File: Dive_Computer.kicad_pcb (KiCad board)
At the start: 2 copper layers, 4 parts, among them IC1 LTC4120EUD-4.2#PBF, IC2 MS583730BA01-50, U1 ESP32-C3_SUPERMINI_TH

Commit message: Schematic update
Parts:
- added BATTERIE1: BAT, Connector_Hirose:Hirose_DF13-02P-1.25DSA_1x02_P1.25mm_Vertical, F.Cu at (142.6, 100.2)
- added C1: 10u, Capacitor_SMD:C_1210_3225Metric, F.Cu at (142.9, 104.5)
- added C10: 100n, Capacitor_SMD:C_0603_1608Metric, F.Cu at (146.1, 83.1)
- added C2: 100n, Capacitor_SMD:C_0603_1608Metric, F.Cu at (142.1, 83.1)
- added C3: 10u, Capacitor_SMD:C_1210_3225Metric, F.Cu at (142.9, 108.8)
- added C4: 26.7n, Capacitor_SMD:C_0603_1608Metric, F.Cu at (142.1, 85.6)
- added C5: 6.5n, Capacitor_SMD:C_0603_1608Metric, F.Cu at (142.1, 88.2)
- added C6: 22u, Capacitor_SMD:C_1210_3225Metric, F.Cu at (142.9, 113.0)
- added C7: 22n, Capacitor_SMD:C_0603_1608Metric, F.Cu at (142.1, 90.7)
- added C8: 2.2u, Capacitor_SMD:C_0603_1608Metric, F.Cu at (142.1, 93.2)
- added C9: 100n, Capacitor_SMD:C_0603_1608Metric, F.Cu at (142.1, 95.7)
- added D1: MSS2P2-M3/89A, Diode_SMD:D_MicroSMP_LargeCathode, F.Cu at (154.8, 83.3)
- added D2: MSS2P2-M3/89A, Diode_SMD:D_MicroSMP_LargeCathode, F.Cu at (154.8, 86.2)
- added D3: MSS2P2-M3/89A, Diode_SMD:D_MicroSMP_LargeCathode, F.Cu at (154.8, 89.0)
- added D4: MSS2P2-M3/89A, Diode_SMD:D_MicroSMP_LargeCathode, F.Cu at (154.8, 91.9)
- added J1: SCREEN, Connector_Hirose:Hirose_DF13-07P-1.25DSA_1x07_P1.25mm_Vertical, F.Cu at (123.0, 110.7)
- added JP1: SolderJumper_2_Open, Jumper:SolderJumper-2_P1.3mm_Open_RoundedPad1.0x1.5mm, F.Cu at (153.0, 114.2)
- added L1: 15u, Inductor_SMD:L_APV_ANR4018, F.Cu at (148.6, 105.2)
- added Power_Inductor1: 47.0 uH, Connector_PinHeader_2.54mm:PinHeader_1x02_P2.54mm_Vertical, F.Cu at (109.8, 109.8)
- added Q1: Si2301HDS, Package_TO_SOT_SMD:TSOT-23, F.Cu at (154.1, 104.8)
- added R1: 10k, Resistor_SMD:R_0603_1608Metric, F.Cu at (146.1, 85.6)
- added R10: 10k, Resistor_SMD:R_0603_1608Metric, F.Cu at (150.1, 93.2)
- added R2: 10k, Resistor_SMD:R_0603_1608Metric, F.Cu at (146.1, 88.2)
- added R3: 3k, Resistor_SMD:R_0603_1608Metric, F.Cu at (146.1, 90.7)
- added R4: 300k, Resistor_SMD:R_0603_1608Metric, F.Cu at (146.1, 93.2)
- added R5: 100k, Resistor_SMD:R_0603_1608Metric, F.Cu at (146.1, 95.7)
- added R6: 10k, Resistor_SMD:R_0603_1608Metric, F.Cu at (150.1, 83.1)
- added R7: 10k, Resistor_SMD:R_0603_1608Metric, F.Cu at (150.1, 85.6)
- added R8: 10k, Resistor_SMD:R_0603_1608Metric, F.Cu at (150.1, 88.2)
- added R9: 10k, Resistor_SMD:R_0603_1608Metric, F.Cu at (150.1, 90.7)
- added U2: Si7201-03-IV, Package_TO_SOT_SMD:SOT-23, F.Cu at (153.3, 110.2)
- IC1: footprint SamacSys_Parts:QFN50P300X300X80-17N-D -> Package_DFN_QFN:QFN-16-1EP_3x3mm_P0.5mm_EP1.7x1.7mm
- IC2: footprint SamacSys_Parts:MS583730BA0150 -> Sensor_Pressure:TE_MS5837-xxBA
- moved U1 67.7 mm to (113.5, 80.9)
- moved IC2 42.1 mm to (148.4, 110.6)
- moved IC1 38.7 mm to (149.3, 99.6)
- moved LIS12DUX1 24.8 mm to (162.3, 109.7)
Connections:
- IC1 pad 1: unconnected-(IC1-INTVCC-Pad1) -> Net-(IC1-FREQ)
- IC1 pad 10: unconnected-(IC1-BATSNS-Pad10) -> VCC
- IC1 pad 12: unconnected-(IC1-NTC-Pad12) -> GND
- IC1 pad 13: unconnected-(IC1-PROG-Pad13) -> Net-(IC1-PROG)
- IC1 pad 14: unconnected-(IC1-~{CHRG}-Pad14) -> /~{CHRG}
- IC1 pad 15: unconnected-(IC1-~{FAULT}-Pad15) -> /~{FLT}
- IC1 pad 16: unconnected-(IC1-RUN-Pad16) -> Net-(D2-K)
- IC1 pad 17: unconnected-(IC1-GND_2-Pad17) -> GND
- IC1 pad 2: unconnected-(IC1-BOOST-Pad2) -> Net-(IC1-BOOST)
- IC1 pad 3: unconnected-(IC1-IN-Pad3) -> Net-(D2-K)
- IC1 pad 4: unconnected-(IC1-SW-Pad4) -> Net-(IC1-SW)
- IC1 pad 5: unconnected-(IC1-GND_1-Pad5) -> GND
- IC1 pad 6: unconnected-(IC1-DHC-Pad6) -> Net-(D2-A)
- IC1 pad 7: unconnected-(IC1-FREQ-Pad7) -> Net-(IC1-FREQ)
- IC1 pad 8: unconnected-(IC1-CHGSNS-Pad8) -> Net-(IC1-CHGSNS)
- IC1 pad 9: unconnected-(IC1-BAT-Pad9) -> VCC
- IC2 pad 1: unconnected-(IC2-GND-Pad1) -> GND
- IC2 pad 2: unconnected-(IC2-VDD-Pad2) -> +3.3V
- IC2 pad 3: unconnected-(IC2-SCL-Pad3) -> /SCL
- IC2 pad 4: unconnected-(IC2-SDA-Pad4) -> /SDA
- LIS12DUX1 pad 1: unconnected-(LIS12DUX1-SCL-Pad1) -> /SCL
- LIS12DUX1 pad 10: unconnected-(LIS12DUX1-Vdd_IO-Pad10) -> +3.3V
- LIS12DUX1 pad 11: unconnected-(LIS12DUX1-INT2-Pad11) -> /INT2
- LIS12DUX1 pad 12: unconnected-(LIS12DUX1-INT1-Pad12) -> /INT1
- LIS12DUX1 pad 2: unconnected-(LIS12DUX1-CS-Pad2) -> +3.3V
- LIS12DUX1 pad 3: unconnected-(LIS12DUX1-SDO-Pad3) -> +3.3V
- LIS12DUX1 pad 4: unconnected-(LIS12DUX1-SDA-Pad4) -> /SDA
- LIS12DUX1 pad 6: unconnected-(LIS12DUX1-GND-Pad6) -> GND
- LIS12DUX1 pad 7: unconnected-(LIS12DUX1-RES-Pad7) -> GND
- LIS12DUX1 pad 8: unconnected-(LIS12DUX1-GND-Pad8) -> GND
- LIS12DUX1 pad 9: unconnected-(LIS12DUX1-Vdd-Pad9) -> +3.3V
- U1 pad 0: unconnected-(U1-GPIO0-Pad0) -> /INT1
- U1 pad 1: unconnected-(U1-GPIO1-Pad1) -> /INT2
- U1 pad 10: unconnected-(U1-GPIO10-Pad10) -> /Data/Command
- U1 pad 20: unconnected-(U1-GPIO20-Pad20) -> /~{CHRG}
- U1 pad 21: unconnected-(U1-GPIO21-Pad21) -> Net-(JP1-A)
- U1 pad 3: unconnected-(U1-GPIO3-Pad3) -> Net-(U1-GPIO3)
- U1 pad 3.3: unconnected-(U1-3V3-Pad3.3) -> +3.3V
- U1 pad 4: unconnected-(U1-GPIO4-Pad4) -> /SPI_CLK
- U1 pad 5: unconnected-(U1-GPIO5-Pad5) -> /MISO
- U1 pad 5V: unconnected-(U1-Pad5V) -> Net-(D4-K)
- U1 pad 6: unconnected-(U1-GPIO6-Pad6) -> /MOSI
- U1 pad 7: unconnected-(U1-GPIO7-Pad7) -> /CS
- U1 pad 8: unconnected-(U1-GPIO8-Pad8) -> /SDA
- U1 pad 9: unconnected-(U1-GPIO9-Pad9) -> /SCL
- U1 pad G: unconnected-(U1-GND-PadG) -> GND

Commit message: Routage terminé
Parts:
- added ?: , , F.Cu at (206.7, 55.5)
- added ?: , , F.Cu at (244.8, 55.5)
- added ?: , , F.Cu at (206.7, 86.0)
- added ?: , , F.Cu at (244.8, 86.0)
- added G***: LOGO, LOGO, B.Cu at (223.0, 74.3)
- C1, C6: footprint Capacitor_SMD:C_1210_3225Metric -> Capacitor_SMD:C_0603_1608Metric
- IC2: moved to B.Cu
- moved U1 120.7 mm to (233.8, 70.7), turned to -90 degrees
- moved Power_Inductor1 113.5 mm to (220.7, 85.6), turned to -90 degrees
- moved J1 113.1 mm to (221.9, 55.9)
- moved IC2 103.2 mm to (237.5, 58.5), turned to -90 degrees
- moved C3 98.1 mm to (238.1, 85.0)
- moved C10 95.5 mm to (237.5, 55.3)
- moved C8 93.1 mm to (234.4, 80.8)
- moved R4 93.1 mm to (238.5, 81.7), turned to 90 degrees
- moved C6 93.0 mm to (232.1, 86.7)
- moved R2 93.0 mm to (234.4, 59.0), turned to 90 degrees
- moved R6 92.1 mm to (242.2, 81.6), turned to -90 degrees
- moved R5 91.9 mm to (236.9, 81.7), turned to -90 degrees
- moved JP1 91.0 mm to (225.9, 59.8), turned to 90 degrees
- moved R7 90.6 mm to (240.6, 81.6), turned to 90 degrees
- moved R1 90.6 mm to (232.7, 58.9), turned to 90 degrees
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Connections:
- C3 pad 1: Net-(D2-K) -> Net-(IC1-RUN)
- IC1 pad 16: Net-(D2-K) -> Net-(IC1-RUN)
- J1 pad 2: /BAT+ -> VCC
- Power_Inductor1 pad 1: Net-(C4-Pad1) -> GND
- Power_Inductor1 pad 2: GND -> Net-(C4-Pad1)
- R4 pad 1: Net-(D2-K) -> Net-(IC1-RUN)
- R5 pad 2: Net-(D2-K) -> Net-(IC1-RUN)
- R6 pad 2: /BAT+ -> VCC
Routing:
- net /SCL: track 0.00 -> 50.5 mm
- net VCC: track 0.00 -> 42.5 mm, vias 0 -> 5
- net /SDA: track 0.00 -> 34.4 mm
- net /~{FLT}: track 0.00 -> 32.0 mm, vias 0 -> 2
- net /~{CHRG}: track 0.00 -> 28.6 mm, vias 0 -> 1
- net /SPI_CLK: track 0.00 -> 26.7 mm
- net /INT2: track 0.00 -> 26.5 mm
- net /INT1: track 0.00 -> 21.2 mm
- net /MISO: track 0.00 -> 20.4 mm
- net Net-(D2-K): track 0.00 -> 19.9 mm, vias 0 -> 3
- net Net-(Q1-G): track 0.00 -> 18.7 mm
- net Net-(D2-A): track 0.00 -> 17.0 mm
- net /MOSI: track 0.00 -> 15.8 mm
- net /CS: track 0.00 -> 15.7 mm
- net Net-(U1-GPIO3): track 0.00 -> 13.0 mm
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- added copper zone on F.Cu, net +3.3V
- added copper zone on In1.Cu, net +3.3V
- added copper zone on F.Cu, net /BAT+
- added copper zone on B.Cu, net GND
- added copper zone on F.Cu, net GND
- added copper zone on In1.Cu, net GND
- added copper zone on In2.Cu, net GND
- added copper zone on F.Cu, net Net-(C4-Pad1)
- added copper zone on F.Cu, net Net-(D1-K)
- added copper zone on F.Cu, net Net-(D2-K)
- added copper zone on In2.Cu, net Net-(D2-K)
- added copper zone on F.Cu, net Net-(D4-K)
- added copper zone on F.Cu, net Net-(IC1-CHGSNS)
- added copper zone on F.Cu, net Net-(IC1-RUN)
- added copper zone on F.Cu, net Net-(IC1-SW)
- added copper zone on F.Cu, net VCC
- added copper zone on In1.Cu, net VCC
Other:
- board outline added: 42.1 x 34.5 mm
- copper layers 2 -> 4
- board text added: "ESP32C3 SUPERMINI"
- board text added: "Freediving Computer V1 Design by Bilal Yousfi"

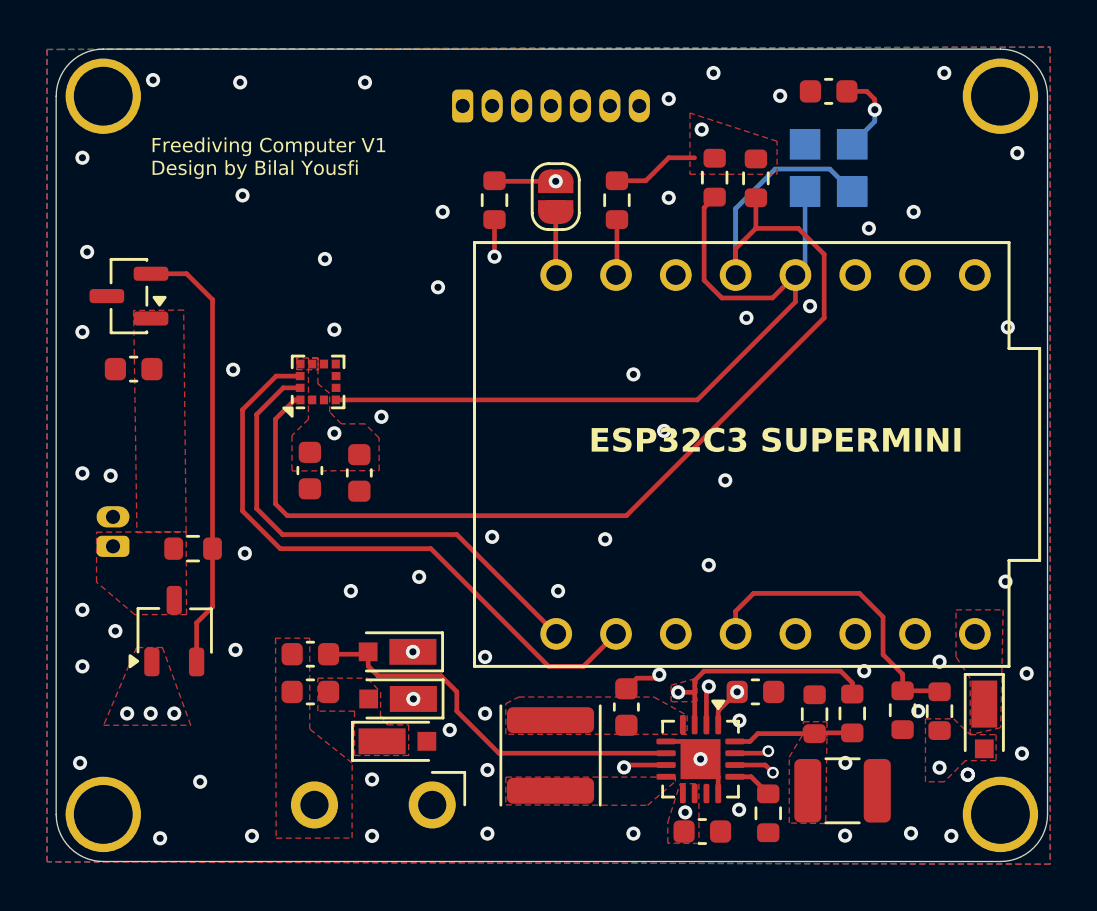
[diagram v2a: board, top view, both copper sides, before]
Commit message: Added 3D models
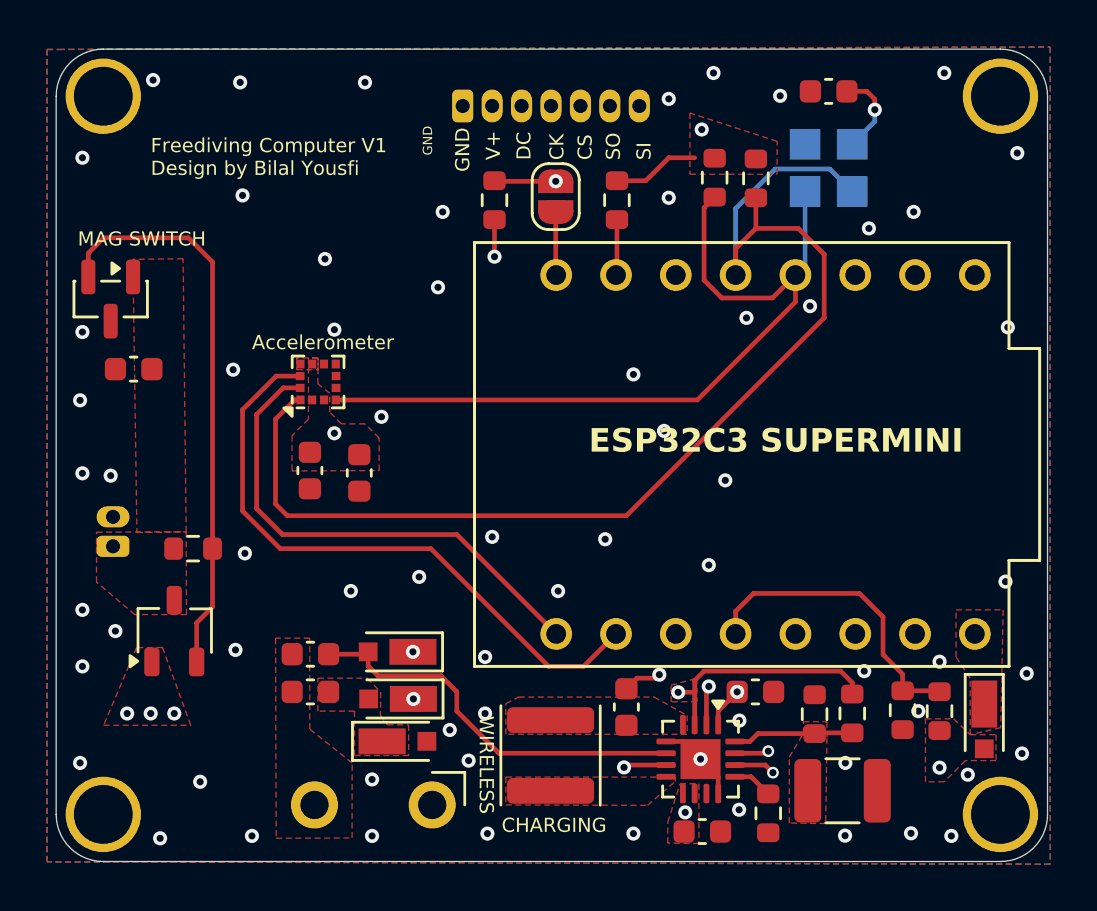
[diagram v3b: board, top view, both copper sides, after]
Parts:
- moved U2 0.79 mm to (207.0, 64.1), turned to -90 degrees
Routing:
- net Net-(Q1-G): track 18.7 -> 24.2 mm
- net GND: vias 67 -> 66
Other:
- board text added: "Accelerometer"
- board text added: "CHARGING"
- board text added: "CK"
- board text added: "CS"
- board text added: "DC"
- board text added: "GND"
- board text added: "MAG SWITCH"
- board text added: "SI"
- board text added: "SO"
- board text added: "V+"
- board text added: "WIRELESS"

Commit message: UI
The UI is mostly done
The core architecture is up and running
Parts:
- moved U2 0.10 mm to (207.0, 64.0)
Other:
- board text removed: "Accelerometer"
- board text removed: "CHARGING"
- board text removed: "CK"
- board text removed: "CS"
- board text removed: "DC"
- board text removed: "GND"
- board text removed: "MAG SWITCH"
- board text removed: "SI"
- board text removed: "SO"
- board text removed: "V+"
- board text removed: "WIRELESS"
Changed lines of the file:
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@@
 			(outputformat 1)
 			(mirror no)
-			(drillshape 0)
+			(drillshape 1)
 			(scaleselection 1)
 			(outputdirectory "")
@@
 			)
 		)
-		(model "${KIPRJMOD}/3d files/MSMP20A-M3_89A.STEP"
+		(model "${KICAD10_3DMODEL_DIR}/Custom/MSMP20A-M3_89A.STEP"
 			(offset
 				(xyz 0 0 0)
@@
 	(footprint "Package_TO_SOT_SMD:SOT-23"
 		(layer "F.Cu")
-		(at 207 64.1 -90)
+		(at 207 64 -90)
 		(descr "SOT, 3 Pin (JEDEC TO-236 Var AB https://www.jedec.org/document_search?search_api_views_fulltext=TO-236)")
 		(tags "SOT TO_SOT_SMD")
@@
 		)
 		(embedded_fonts no)
-		(model "${KIPRJMOD}/3d files/ESP32-C3 SuperMini_TH--3DModel-STEP-56544.STEP"
+		(model "${KICAD10_3DMODEL_DIR}/Custom/ESP32-C3 SuperMini_TH--3DModel-STEP-56544.STEP"
 			(offset
 				(xyz 0 0 0)
@@
 			)
 			(rotate
-				(xyz 0 0 0)
+				(xyz -90 -0 -0)
 			)
 		)
-		(model "${KIPRJMOD}/3d files/MSMP20A-M3_89A.STEP"
+		(model "${KICAD10_3DMODEL_DIR}/Custom/MSMP20A-M3_89A.STEP"
 			(offset
 				(xyz 0 0 0)
@@
 			)
 		)
-		(model "${KIPRJMOD}/3d files/MSMP20A-M3_89A.STEP"
+		(model "${KICAD10_3DMODEL_DIR}/Custom/MSMP20A-M3_89A.STEP"
 			(offset
 				(xyz 0 0 0)
@@
 			)
 		)
-		(model "${KIPRJMOD}/3d files/MSMP20A-M3_89A.STEP"
+		(model "${KICAD10_3DMODEL_DIR}/Custom/MSMP20A-M3_89A.STEP"
 			(offset
 				(xyz 0 0 0)
@@
 			)
 		)
-		(model "${KIPRJMOD}/3d files/MS583730BA01-50--3DModel-STEP-510211.STEP"
+		(model "${KICAD10_3DMODEL_DIR}/Custom/MS583730BA01-50--3DModel-STEP-510211.STEP"
 			(offset
 				(xyz 0 0 0)
@@
 		(layer "B.Fab")
 	)
-	(gr_text "GND"
-		(at 220.7 58 90)
-		(layer "F.SilkS")
-		(effects
-			(font
-				(size 0.4 0.4)
-			)
-			(justify left bottom)
-		)
-	)
-	(gr_text "MAG SWITCH"
-		(at 205.6 61.9 0)
-		(layer "F.SilkS")
-		(effects
-			(font
-				(size 0.6 0.6)
-			)
-			(justify left bottom)
-		)
-	)
 	(gr_text "Freediving Computer V1\nDesign by Bilal Yousfi"
 		(at 208.7 58.9 0)
@@
 		)
 	)
-	(gr_text "Accelerometer"
-		(at 213 66.3 0)
-		(layer "F.SilkS")
-		(effects
-			(font
-				(size 0.6 0.6)
-			)
-			(justify left bottom)
-		)
-	)
-	(gr_text "CHARGING"
-		(at 223.6 86.8 0)
-		(layer "F.SilkS")
-		(effects
-			(font
-				(size 0.6 0.6)
-			)
-			(justify left bottom)
-		)
-	)
-	(gr_text "GND"
-		(at 222.3 58.7 90)
-		(layer "F.SilkS")
-		(effects
-			(font
-				(size 0.6 0.6)
-			)
-			(justify left bottom)
-		)
-	)
-	(gr_text "V+"
-		(at 223.6 58.2 90)
-		(layer "F.SilkS")
-		(effects
-			(font
-				(size 0.6 0.6)
-			)
-			(justify left bottom)
-		)
-	)
-	(gr_text "DC"
-		(at 224.9 58.2 90)
-		(layer "F.SilkS")
-		(effects
-			(font
-				(size 0.6 0.6)
-			)
-			(justify left bottom)
-		)
-	)
-	(gr_text "CK"
-		(at 226.3 58.2 90)
-		(layer "F.SilkS")
-		(effects
-			(font
-				(size 0.6 0.6)
-			)
-			(justify left bottom)
-		)
-	)
-	(gr_text "CS"
-		(at 227.5 58.2 90)
-		(layer "F.SilkS")
-		(effects
-			(font
-				(size 0.6 0.6)
-			)
-			(justify left bottom)
-		)
-	)
-	(gr_text "SO"
-		(at 228.7 58.2 90)
-		(layer "F.SilkS")
-		(effects
-			(font
-				(size 0.6 0.6)
-			)
-			(justify left bottom)
-		)
-	)
-	(gr_text "SI"
-		(at 230 58.2 90)
-		(layer "F.SilkS")
-		(effects
-			(font
-				(size 0.6 0.6)
-			)
-			(justify left bottom)
-		)
-	)
-	(gr_text "WIRELESS"
-		(at 222.6 81.8 270)
-		(layer "F.SilkS")
-		(effects
-			(font
-				(size 0.6 0.6)
-			)
-			(justify left bottom)
-		)
-	)
 	(gr_text "ESP32C3 SUPERMINI"
 		(at 227.3 70.7 0)
@@
 	)
 	(via
+		(at 205.8 65.5)
+		(size 0.6)
+		(drill 0.3)
+		(layers "F.Cu" "B.Cu")
+		(free yes)
+		(net "GND")
+	)
+	(via
 		(at 222.9 81.7)
 		(size 0.6)
@@
 	)
 	(via
-		(at 205.7 68.4)
-		(size 0.6)
-		(drill 0.3)
-		(layers "F.Cu" "B.Cu")
-		(free yes)
-		(net "GND")
-	)
-	(via
 		(at 245.7 83.4)
 		(size 0.6)
@@
 	)
 	(via
+		(at 243.4 84.3)
+		(size 0.6)
+		(drill 0.3)
+		(layers "F.Cu" "B.Cu")
+		(free yes)
+		(net "GND")
+	)
+	(via
 		(at 242.4 54.5)
 		(size 0.6)
@@
 	)
 	(via
-		(at 222.2 83.7)
+		(at 223 84.1)
 		(size 0.6)
 		(drill 0.3)
@@
 	)
 	(via
-		(at 205.8 65.5)
-		(size 0.6)
-		(drill 0.3)
-		(layers "F.Cu" "B.Cu")
-		(free yes)
-		(net "GND")
-	)
-	(via
 		(at 230.5 69.7)
 		(size 0.6)
@@
 	)
 	(segment
-		(start 211.324999 74.7)
-		(end 211.324999 62.524999)
+		(start 206.6 61.5)
+		(end 206.05 62.05)
 		(width 0.2)
 		(layer "F.Cu")
@@
 	)
 	(segment
-		(start 206.7 61.5)
-		(end 206.05 62.15)
+		(start 210.3 61.5)
+		(end 206.6 61.5)
 		(width 0.2)
 		(layer "F.Cu")
@@
 	)
 	(segment
-		(start 211.324999 62.524999)
-		(end 210.3 61.5)
+		(start 206.05 62.05)
+		(end 206.05 63.0625)
 		(width 0.2)
 		(layer "F.Cu")
@@
 	)
 	(segment
-		(start 206.05 62.15)
-		(end 206.05 63.1625)
+		(start 211.324999 74.7)
+		(end 211.324999 62.524999)
 		(width 0.2)
 		(layer "F.Cu")
@@
 	)
 	(segment
-		(start 210.3 61.5)
-		(end 206.7 61.5)
+		(start 211.324999 62.524999)
+		(end 210.3 61.5)
 		(width 0.2)
 		(layer "F.Cu")
@@
 		(polygon
 			(pts
-				(xy 207.943918 62.411883) (xy 208.115039 74.014759) (xy 210.205819 73.983924) (xy 210.075351 62.387901)
+				(xy 207.942443 62.311899) (xy 208.115039 74.014759) (xy 210.205819 73.983924) (xy 210.074226 62.287913)
 			)
 		)
